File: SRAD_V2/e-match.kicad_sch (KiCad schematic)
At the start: 39 parts, among them IC1 NCV81071BZR2G, IC2 NCV81071BZR2G, J2 691210910002, J3 691210910002, J4 691210910002, J5 691210910002, Q1 AOSP36326C, Q2 AOSP36326C, Q3 NTMFS5C673NT1G, Q4 NTMFS5C673NT1G, U3 TMCS1108A2UQDR

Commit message: more routing
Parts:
- removed C89: 6.8mF, Capacitor_THT:CP_Radial_D16.0mm_P7.50mm, symbol Device:C_Polarized
- removed L3: IHLP4040DZER6R8M01, 6.8uH Inductor:IND_IHLP-4040DZ_VIS, symbol 6.8uH Inductor:IHLP4040DZER6R8M01
- removed LED1: LTST-C170GKT, Smd_Led:LED_LTST-C170GKT_LTO, symbol LTST-C170GKT:LTST-C170GKT
- removed Q1, Q2: AOSP36326C, Package_SO:SOIC-8_3.9x4.9mm_P1.27mm, symbol Transistor_FET:FDS6630A
- removed R7: 330R, Resistor_SMD:R_0603_1608Metric, symbol RC0603JR-07330RL:RC0603JR-07330RL
- removed R89: 100m, Resistor_SMD:R_1206_3216Metric, symbol Device:R_Small
- added C13, C14: 10u, Capacitor_SMD:C_1210_3225Metric, symbol Device:C_Small
- added Q1, Q2: NTMFS5C673NT1G, NTMFS5C673NT1G-2:TRANS_NTMFS5C673NT1G, symbol NTMFS5C673NT1G:NTMFS5C673NT1G
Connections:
- net +BATT is gone; now on net Vf: C5.1, C6.1, C8.1, C9.1, IC1.8 (VDD), IC2.8 (VDD)
- net Drain1: now also Q1.5
- net Drain2: now also Q2.5
- net GND: now also C13.2, C14.2, Q1.1, Q1.2, Q1.3, Q2.1, Q2.2, Q2.3
- net Vf: now also C13.1, C14.1
- net at R3.1: now also Q1.4
- net at R4.1: now also Q2.4
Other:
- note removed: "Low pass LC filter with a damping leg"
- moved on the sheet: R3, R4

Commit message: more layout optimisation
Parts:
- added J6: 691210910002, Screw_Terminal:691210910002, symbol Screw Terminal:691210910002
- renumbered J2 to EM1, J3 to EM2, J4 to EM3, J5 to EM4
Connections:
- net GND: now also J6.2
- net IN(-): now also C13.1, C14.1
- net Vf renamed +BATT
- net +BATT: now also J6.1; no longer C13.1, C14.1
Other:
- moved on the sheet: C13, C14

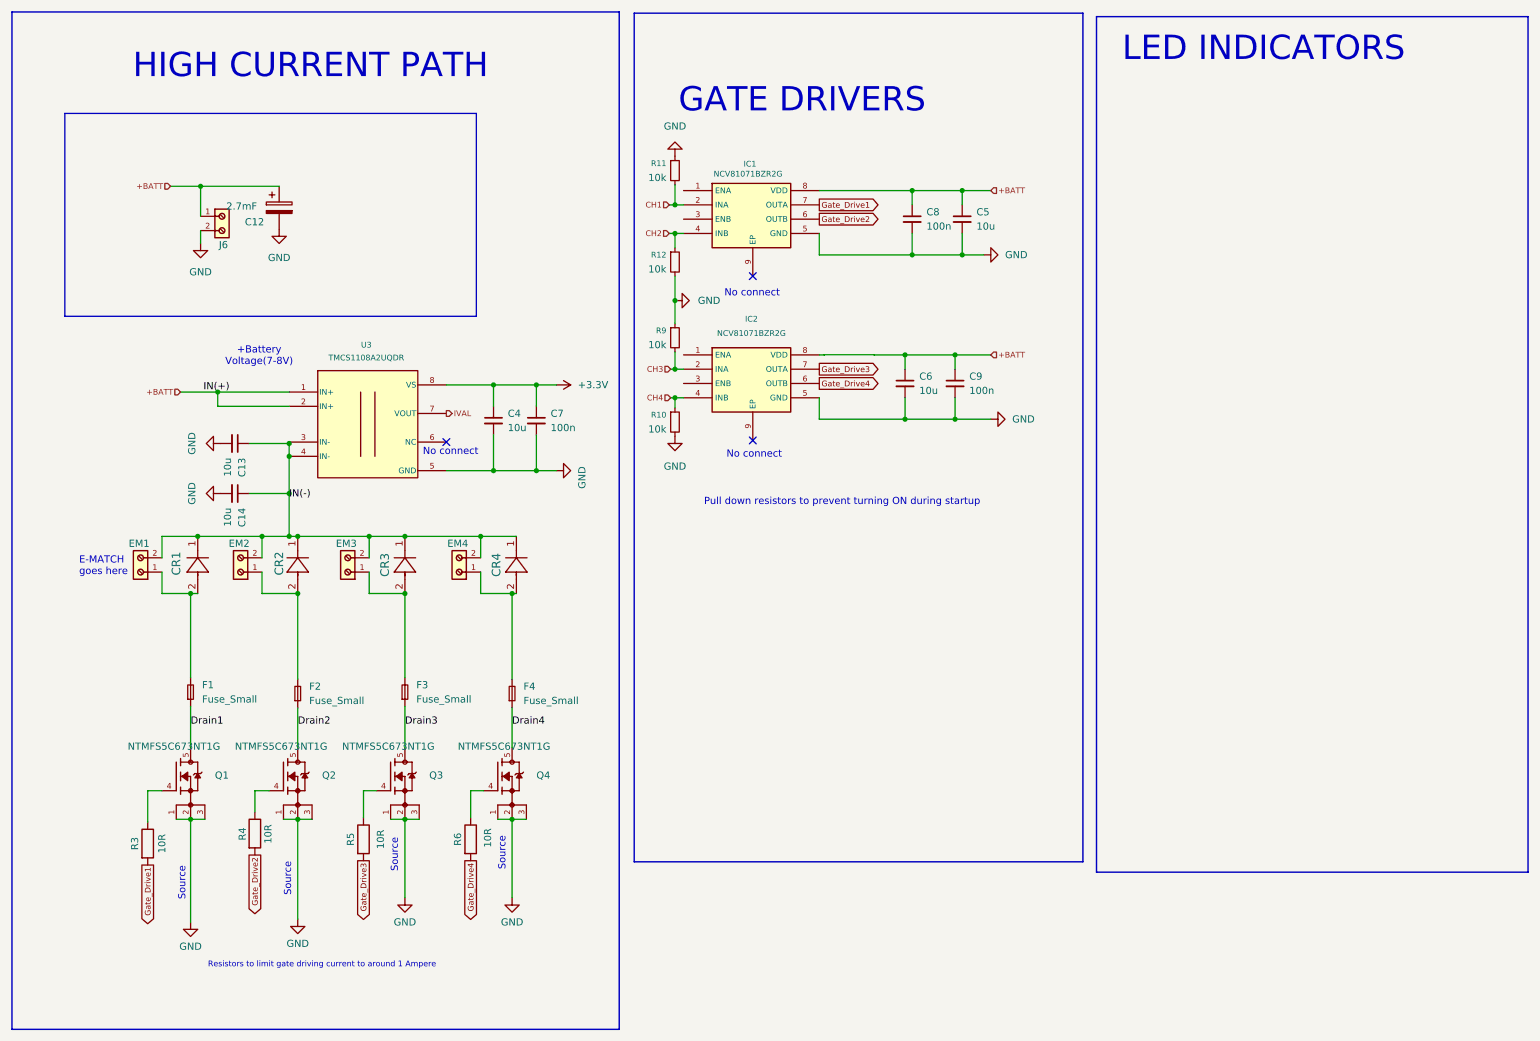
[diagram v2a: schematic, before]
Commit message: Added important GPS circuitry
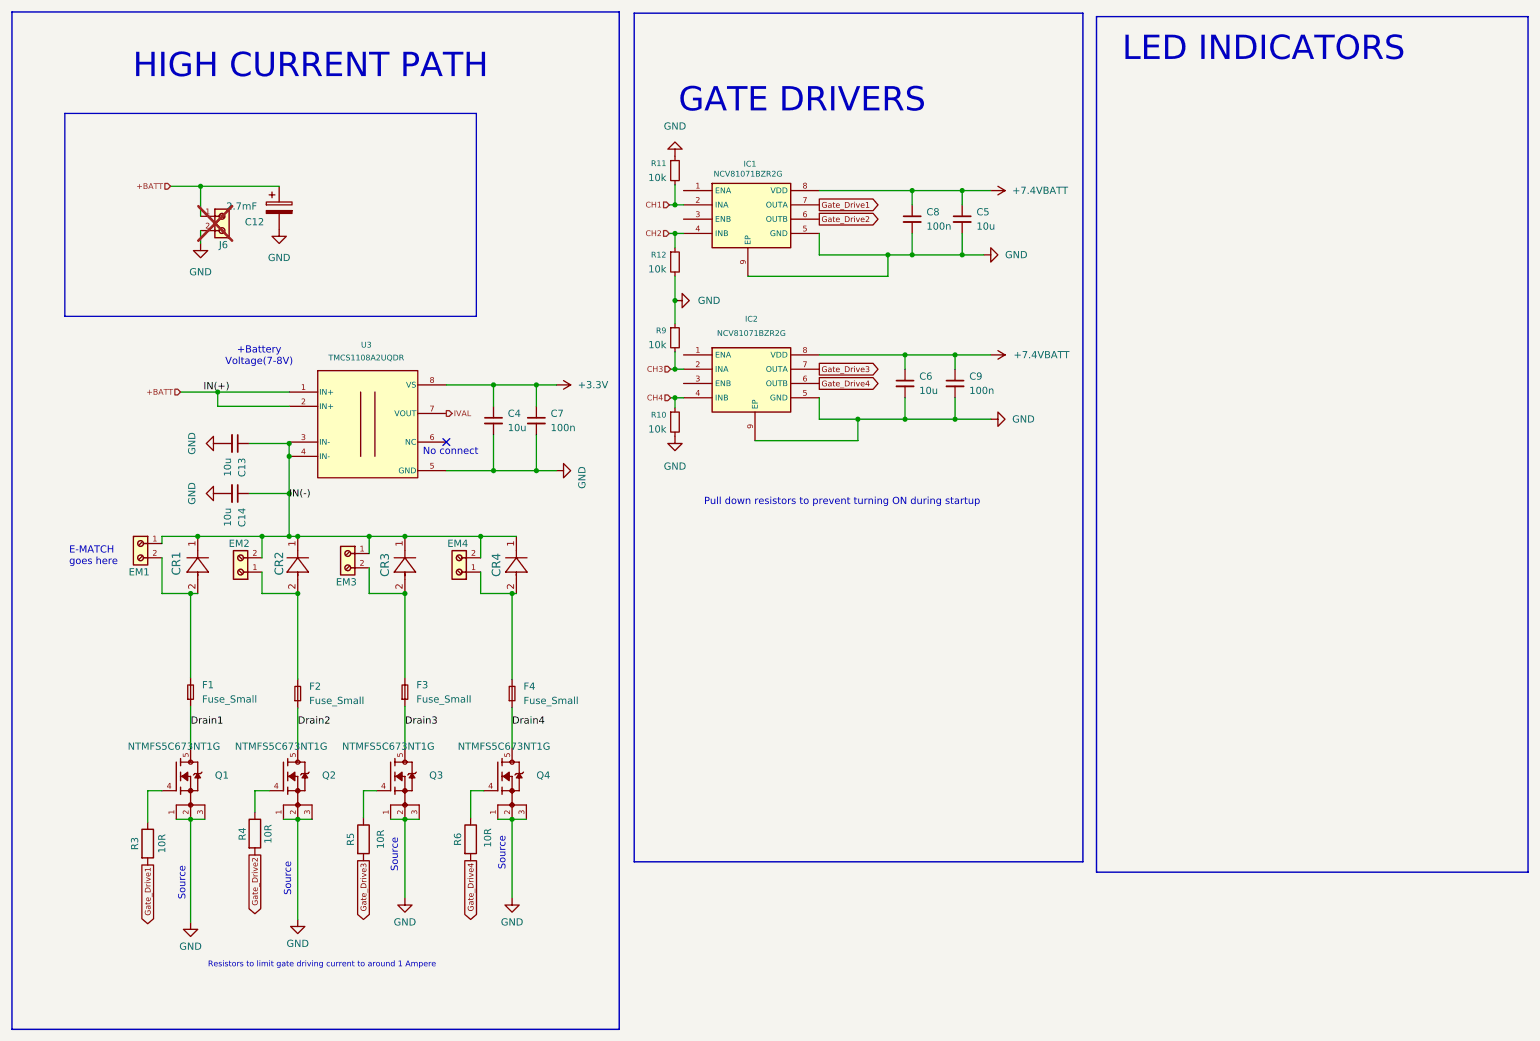
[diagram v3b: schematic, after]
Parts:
- C4: footprint Capacitor_SMD:C_0603_1608Metric -> Capacitor_SMD:C_1210_3225Metric
- J6: now not fitted
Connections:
- net +BATT: no longer C5.1, C6.1, C8.1, C9.1, IC1.8 (VDD), IC2.8 (VDD)
- net GND: now also IC1.9 (EP), IC2.9 (EP)
- net IN(-): now also EM1.1, EM3.1; no longer EM1.2, EM3.2
- net at CR3.2, F3.2: now also EM3.2; no longer EM3.1
- net at CR1.2, F1.2: now also EM1.2; no longer EM1.1
- new net +7.4VBATT: C5.1, C6.1, C8.1, C9.1, IC1.8 (VDD), IC2.8 (VDD)
- no-connect marks 3 -> 1
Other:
- moved on the sheet: EM1, EM3

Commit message: Focusing on signal integrity and shielding now!
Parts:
- removed J6: 691210910002, Screw_Terminal:691210910002, symbol Screw Terminal:691210910002

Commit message: ensuring proper grounding in the layout
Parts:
- R10, R11, R12, R9: footprint (none) -> Resistor_SMD:R_0402_1005Metric
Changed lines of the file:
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@@
 			)
 		)
-		(property "Footprint" ""
+		(property "Footprint" "Resistor_SMD:R_0402_1005Metric"
 			(at 131.826 84.328 0)
 			(hide yes)
@@
 			)
 		)
-		(property "Footprint" ""
+		(property "Footprint" "Resistor_SMD:R_0402_1005Metric"
 			(at 131.826 39.624 0)
 			(hide yes)
@@
 			)
 		)
-		(property "Footprint" ""
+		(property "Footprint" "Resistor_SMD:R_0402_1005Metric"
 			(at 131.826 69.342 0)
 			(hide yes)
@@
 			)
 		)
-		(property "Footprint" ""
+		(property "Footprint" "Resistor_SMD:R_0402_1005Metric"
 			(at 131.826 55.88 0)
 			(hide yes)

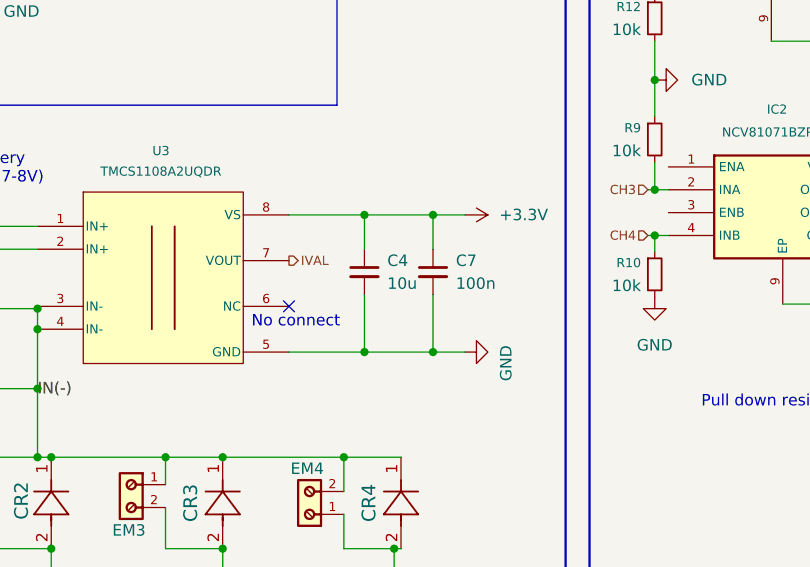
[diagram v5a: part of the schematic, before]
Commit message: Updated IMU sensor and generated Interactive BOM using a plugin
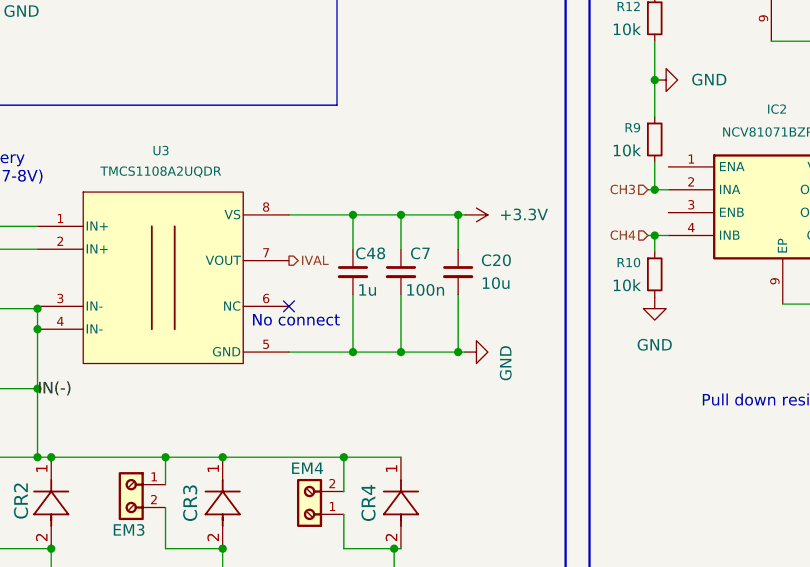
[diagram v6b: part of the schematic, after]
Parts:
- removed C4: 10u, Capacitor_SMD:C_1210_3225Metric, symbol Device:C_Small
- added C20: 10u, Capacitor_SMD:C_1206_3216Metric, symbol Device:C_Small
- added C48: 1u, Capacitor_SMD:C_0603_1608Metric, symbol Device:C_Small
- C13, C14, C5, C6: footprint Capacitor_SMD:C_1210_3225Metric -> Capacitor_SMD:C_1206_3216Metric
- R10, R11, R12, R9: footprint Resistor_SMD:R_0402_1005Metric -> Resistor_SMD:R_0603_1608Metric
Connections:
- net +3.3V: now also C20.1, C48.1
- net GND: now also C20.2, C48.2
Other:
- moved on the sheet: C7

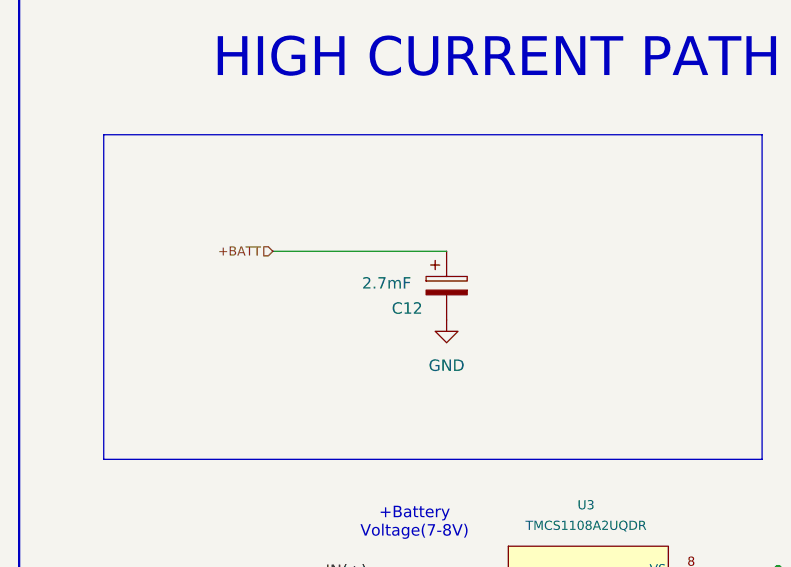
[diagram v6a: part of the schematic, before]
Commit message: Added the JST connectors
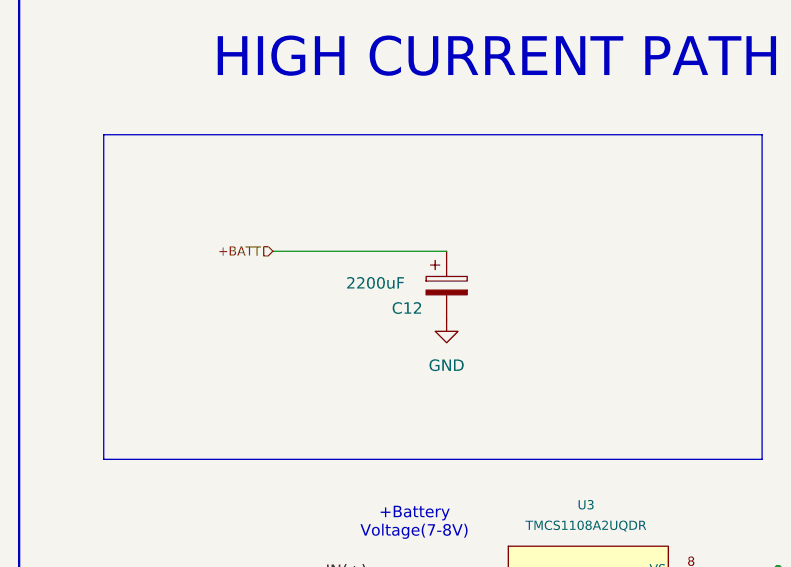
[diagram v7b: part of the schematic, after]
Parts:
- C12: value 2.7mF -> 2200uF
- R3, R4, R5, R6: footprint Resistor_SMD:R_0603_1608Metric -> Resistor_SMD:R_1206_3216Metric
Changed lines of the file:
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@@
 			)
 		)
-		(property "Footprint" "Resistor_SMD:R_0603_1608Metric"
+		(property "Footprint" "Resistor_SMD:R_1206_3216Metric"
 			(at 93.726 158.496 90)
 			(hide yes)
@@
 		(in_bom yes)
 		(on_board yes)
-		(in_pos_files yes)
+		(in_pos_files no)
 		(dnp no)
 		(property "Reference" "EM3"
@@
 		(in_bom yes)
 		(on_board yes)
-		(in_pos_files yes)
+		(in_pos_files no)
 		(dnp no)
 		(property "Reference" "C12"
@@
 			)
 		)
-		(property "Value" "2.7mF"
-			(at 52.07 45.974 0)
+		(property "Value" "2200uF"
+			(at 50.292 45.974 0)
 			(show_name no)
 			(do_not_autoplace no)
@@
 			)
 		)
-		(property "Footprint" "Resistor_SMD:R_0603_1608Metric"
+		(property "Footprint" "Resistor_SMD:R_1206_3216Metric"
 			(at 74.676 158.496 90)
 			(hide yes)
@@
 		(in_bom yes)
 		(on_board yes)
-		(in_pos_files yes)
+		(in_pos_files no)
 		(dnp no)
 		(property "Reference" "EM1"
@@
 			)
 		)
-		(property "Footprint" "Resistor_SMD:R_0603_1608Metric"
+		(property "Footprint" "Resistor_SMD:R_1206_3216Metric"
 			(at 55.372 157.48 90)
 			(hide yes)
@@
 		(in_bom yes)
 		(on_board yes)
-		(in_pos_files yes)
+		(in_pos_files no)
 		(dnp no)
 		(property "Reference" "EM4"
@@
 		(in_bom yes)
 		(on_board yes)
-		(in_pos_files yes)
+		(in_pos_files no)
 		(dnp no)
 		(property "Reference" "EM2"
@@
 			)
 		)
-		(property "Footprint" "Resistor_SMD:R_0603_1608Metric"
+		(property "Footprint" "Resistor_SMD:R_1206_3216Metric"
 			(at 36.322 159.258 90)
 			(hide yes)
